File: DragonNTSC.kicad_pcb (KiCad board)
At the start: 2 copper layers, 120.2 x 35.7 mm, 19 parts, among them IC1 74LS273N, IC2 MC6847, IC3 MC1372, J1 Video Output, J2 Board Interconnect Male, Q1 2N4403, Q2 2N4401

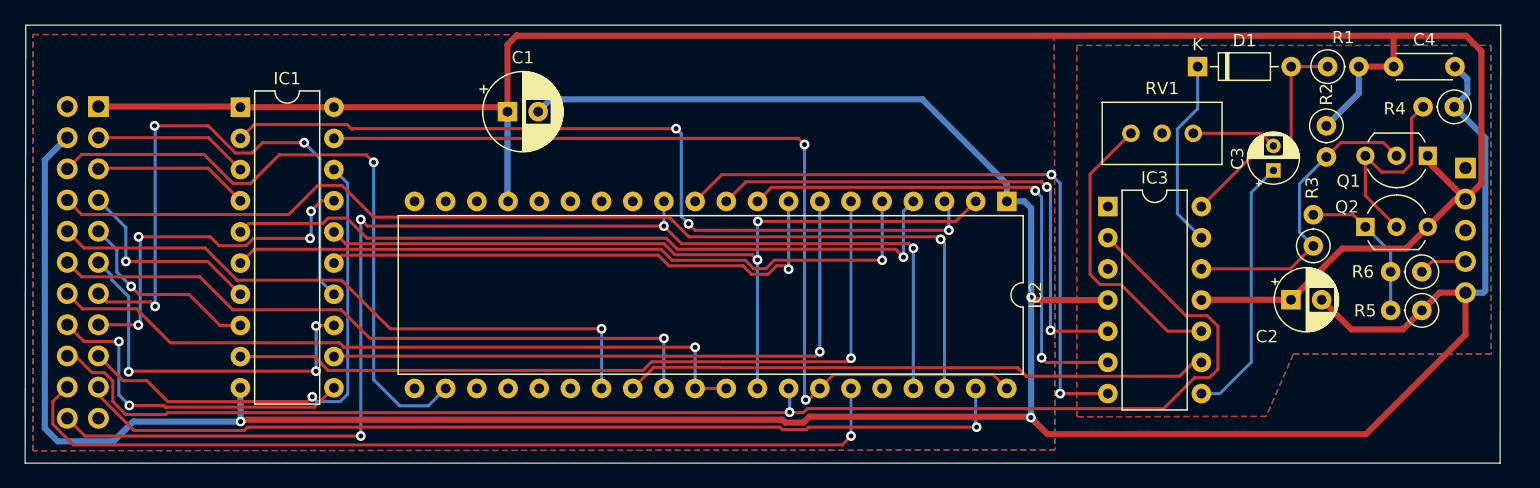
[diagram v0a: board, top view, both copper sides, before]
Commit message: complete tracing for fabrication
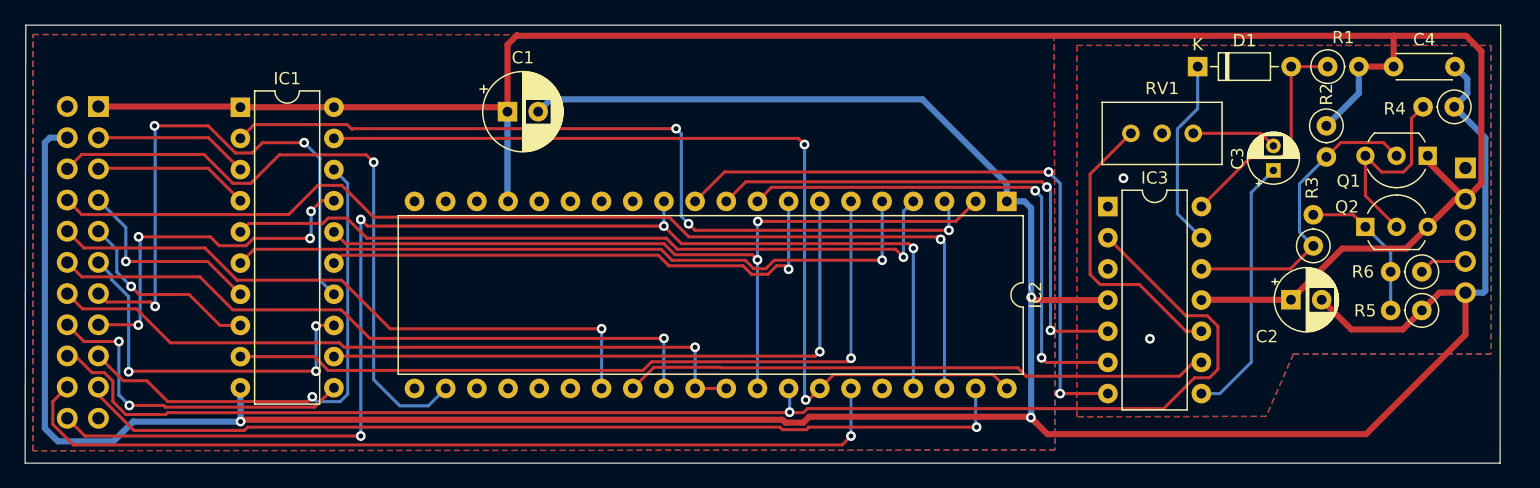
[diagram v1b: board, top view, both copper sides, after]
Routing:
- net GND: track 257.2 -> 258.1 mm, vias 3 -> 5
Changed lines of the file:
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@@
   (segment (start 198.6788 122.2248) (end 198.6788 118.7958) (width 0.5) (layer "F.Cu") (net 2))
   (via (at 163.2712 128.9691) (size 0.8) (drill 0.4) (layers "F.Cu" "B.Cu") (net 2))
+  (via (at 172.974 122.555) (size 0.8) (drill 0.4) (layers "F.Cu" "B.Cu") (free) (net 2))
   (via (at 163.2966 119.1768) (size 0.8) (drill 0.4) (layers "F.Cu" "B.Cu") (net 2))
+  (via (at 170.815 109.474) (size 0.8) (drill 0.4) (layers "F.Cu" "B.Cu") (free) (net 2))
   (via (at 98.8822 129.2993) (size 0.8) (drill 0.4) (layers "F.Cu" "B.Cu") (net 2))
   (segment (start 186.9648 119.8684) (end 186.9648 119.375) (width 0.5) (layer "B.Cu") (net 2))
-  (segment (start 82.931 108.0008) (end 84.7598 106.172) (width 0.5) (layer "B.Cu") (net 2))
   (segment (start 197.826 100.3808) (end 198.8312 101.386) (width 0.5) (layer "B.Cu") (net 2))
+  (segment (start 90.1313 129.2993) (end 88.519 130.9116) (width 0.5) (layer "B.Cu") (net 2))
   (segment (start 98.8822 127.9906) (end 98.8668 127.9752) (width 0.5) (layer "B.Cu") (net 2))
-  (segment (start 83.9978 130.9116) (end 82.931 129.8448) (width 0.5) (layer "B.Cu") (net 2))
   (segment (start 200.3044 106.1938) (end 200.3044 118.618) (width 0.5) (layer "B.Cu") (net 2))
   (segment (start 162.7455 111.3613) (end 161.3154 111.3613) (width 0.5) (layer "B.Cu") (net 2))
   (segment (start 163.2712 128.9691) (end 163.2966 128.9437) (width 0.5) (layer "B.Cu") (net 2))
   (segment (start 198.8312 101.386) (end 198.8312 102.5942) (width 0.5) (layer "B.Cu") (net 2))
-  (segment (start 82.931 129.8448) (end 82.931 108.0008) (width 0.5) (layer "B.Cu") (net 2))
+  (segment (start 83.9978 130.9116) (end 82.931 129.8448) (width 0.5) (layer "B.Cu") (net 2))
   (segment (start 88.519 130.9116) (end 83.9978 130.9116) (width 0.5) (layer "B.Cu") (net 2))
   (segment (start 198.8312 102.5942) (end 197.768 103.6574) (width 0.5) (layer "B.Cu") (net 2))
@@
   (segment (start 163.2966 119.1768) (end 163.2966 111.9124) (width 0.5) (layer "B.Cu") (net 2))
   (segment (start 200.3044 118.618) (end 200.1266 118.7958) (width 0.5) (layer "B.Cu") (net 2))
+  (segment (start 82.931 106.5784) (end 83.3374 106.172) (width 0.5) (layer "B.Cu") (net 2))
+  (segment (start 83.3374 106.172) (end 84.7598 106.172) (width 0.5) (layer "B.Cu") (net 2))
   (segment (start 98.8668 127.9752) (end 98.8668 126.5478) (width 0.5) (layer "B.Cu") (net 2))
+  (segment (start 82.931 129.8448) (end 82.931 106.5784) (width 0.5) (layer "B.Cu") (net 2))
+  (segment (start 98.8822 129.2993) (end 90.1313 129.2993) (width 0.5) (layer "B.Cu") (net 2))
   (segment (start 163.2966 111.9124) (end 162.7455 111.3613) (width 0.5) (layer "B.Cu") (net 2))
   (segment (start 161.3154 109.9312) (end 154.432 103.0478) (width 0.5) (layer "B.Cu") (net 2))
@@
   (segment (start 200.1266 118.7958) (end 198.6788 118.7958) (width 0.5) (layer "B.Cu") (net 2))
   (segment (start 163.2712 128.9691) (end 163.7405 129.4384) (width 0.5) (layer "B.Cu") (net 2))
-  (segment (start 90.1313 129.2993) (end 88.519 130.9116) (width 0.5) (layer "B.Cu") (net 2))
   (segment (start 98.8822 129.2993) (end 98.8822 127.9906) (width 0.5) (layer "B.Cu") (net 2))
   (segment (start 154.432 103.0478) (end 124.1329 103.0478) (width 0.5) (layer "B.Cu") (net 2))
-  (segment (start 98.8822 129.2993) (end 90.1313 129.2993) (width 0.5) (layer "B.Cu") (net 2))
   (segment (start 163.2966 128.9437) (end 163.2966 119.1768) (width 0.5) (layer "B.Cu") (net 2))
   (segment (start 107.5666 105.1028) (end 99.9918 105.1028) (width 0.25) (layer "F.Cu") (net 3))
@@
   (segment (start 164.8706 110.480803) (end 164.8706 121.8692) (width 0.25) (layer "B.Cu") (net 21))
   (segment (start 164.580134 110.190337) (end 164.8706 110.480803) (width 0.25) (layer "B.Cu") (net 21))
-  (segment (start 138.0948 109.1819) (end 135.9154 111.3613) (width 0.25) (layer "F.Cu") (net 22))
-  (segment (start 164.9476 109.1819) (end 138.0948 109.1819) (width 0.25) (layer "F.Cu") (net 22))
+  (segment (start 164.719 108.966) (end 138.3107 108.966) (width 0.25) (layer "F.Cu") (net 22))
   (segment (start 165.6588 127.0204) (end 169.545 127.0204) (width 0.25) (layer "F.Cu") (net 22))
-  (via (at 164.9476 109.1819) (size 0.8) (drill 0.4) (layers "F.Cu" "B.Cu") (net 22))
+  (segment (start 138.3107 108.966) (end 135.9154 111.3613) (width 0.25) (layer "F.Cu") (net 22))
+  (via (at 164.719 108.966) (size 0.8) (drill 0.4) (layers "F.Cu" "B.Cu") (net 22))
   (via (at 165.6588 127.0204) (size 0.8) (drill 0.4) (layers "F.Cu" "B.Cu") (net 22))
-  (segment (start 165.6588 127.0204) (end 165.6588 109.8931) (width 0.25) (layer "B.Cu") (net 22))
-  (segment (start 165.6588 109.8931) (end 164.9476 109.1819) (width 0.25) (layer "B.Cu") (net 22))
+  (segment (start 165.6588 109.9058) (end 165.6588 127.0204) (width 0.25) (layer "B.Cu") (net 22))
+  (segment (start 164.719 108.966) (end 165.6588 109.9058) (width 0.25) (layer "B.Cu") (net 22))
   (segment (start 133.371101 113.3735) (end 134.805601 114.808) (width 0.25) (layer "F.Cu") (net 23))
   (segment (start 153.328824 114.808) (end 153.7004 115.179576) (width 0.25) (layer "F.Cu") (net 23))
@@
   (segment (start 158.7754 126.6013) (end 158.7754 129.6783) (width 0.25) (layer "B.Cu") (net 45))
   (segment (start 158.7754 129.6783) (end 158.8516 129.7545) (width 0.25) (layer "B.Cu") (net 45))
-  (segment (start 168.917105 118.1354) (end 170.6118 118.1354) (width 0.25) (layer "F.Cu") (net 48))
+  (segment (start 171.4246 105.8164) (end 168.0972 109.1438) (width 0.25) (layer "F.Cu") (net 48))
+  (segment (start 168.917105 118.1354) (end 172.1104 118.1354) (width 0.25) (layer "F.Cu") (net 48))
+  (segment (start 172.1104 118.1354) (end 175.9154 121.9404) (width 0.25) (layer "F.Cu") (net 48))
   (segment (start 168.0972 117.315495) (end 168.917105 118.1354) (width 0.25) (layer "F.Cu") (net 48))
+  (segment (start 175.9154 121.9404) (end 177.165 121.9404) (width 0.25) (layer "F.Cu") (net 48))
   (segment (start 168.0972 109.1438) (end 168.0972 117.315495) (width 0.25) (layer "F.Cu") (net 48))
-  (segment (start 170.6118 118.1354) (end 174.4168 121.9404) (width 0.25) (layer "F.Cu") (net 48))
-  (segment (start 171.4246 105.8164) (end 168.0972 109.1438) (width 0.25) (layer "F.Cu") (net 48))
-  (segment (start 174.4168 121.9404) (end 177.165 121.9404) (width 0.25) (layer "F.Cu") (net 48))
   (segment (start 195.9646 116.2558) (end 195.1264 117.094) (width 0.25) (layer "F.Cu") (net 49))
   (segment (start 198.6788 116.2558) (end 195.9646 116.2558) (width 0.25) (layer "F.Cu") (net 49))

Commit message: prepare alpha2 build
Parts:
- added C5: 150pF, Capacitor_THT:C_Rect_L7.0mm_W2.5mm_P5.00mm, F.Cu at (164.4, 130.8)
- added C6: 0.1uF, Capacitor_THT:C_Rect_L7.0mm_W2.5mm_P5.00mm, F.Cu at (149.9, 104.0)
- added FB1: ?uH, Inductor_THT:L_Axial_L7.0mm_D3.3mm_P5.08mm_Vertical_Fastron_MICC, F.Cu at (119.4, 129.6)
- added R7: 150R, Resistor_THT:R_Axial_DIN0207_L6.3mm_D2.5mm_P2.54mm_Vertical, F.Cu at (142.3, 129.2)
- added R8: 10k, Resistor_THT:R_Axial_DIN0207_L6.3mm_D2.5mm_P2.54mm_Vertical, F.Cu at (157.5, 129.5)
- moved R4 8.19 mm to (190.6, 107.6), turned to 0 degrees
- moved R2 5.83 mm to (186.5, 111.0)
- moved C2 5.82 mm to (184.5, 125.2)
- moved D1 5.04 mm to (178.9, 105.0)
- moved C4 4.54 mm to (194.5, 104.6)
- moved R1 4.47 mm to (189.6, 104.3)
- moved C3 3.88 mm to (182.5, 112.7)
- moved R5 3.73 mm to (195.1, 124.0)
- moved Q1 3.45 mm to (195.6, 111.1)
- moved Q2 3.25 mm to (190.6, 116.7)
- moved R6 3.18 mm to (195.1, 120.3)
- moved R3 3.14 mm to (183.7, 116.8), turned to 0 degrees
- moved RV1 1.57 mm to (174.9, 105.8)
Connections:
- net Net-(IC1-Q0) renamed /D0
- net Net-(IC1-Q1) renamed /D1
- net Net-(IC1-Q2) renamed /D2
- net Net-(IC1-Q3) renamed /D3
- net Net-(IC1-Q4) renamed /D4
- net Net-(IC1-Q5) renamed /D5
- net Net-(IC1-Q6) renamed /D6
- net Net-(IC1-Q7) renamed /D7
- IC2 pad 33: VCLK -> Net-(IC2-CLK)
- IC3 pad 2: VCLK -> Net-(IC3-OSC)
- J2 pad 18: VCLK -> Net-(J2-Pin_18)
- RV1 pad 1: Net-(C3-Pad2) -> unconnected-(RV1-Pad1)
- RV1 pad 2: unconnected-(RV1-Pad2) -> Net-(C3-Pad2)
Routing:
- net GND: track 258.1 -> 45.5 mm, vias 5 -> 8
- net +5V: track 180.1 -> 0.00 mm
- net VCLK: track 115.7 -> 34.2 mm, vias 1 -> 0
- net Net-(J2-Pin_18): track 0.00 -> 38.0 mm
- net Net-(IC3-OSC): track 0.00 -> 35.8 mm
- net /D6: track 67.5 -> 86.1 mm, vias 2 -> 3
- net CSS: track 76.9 -> 86.2 mm, vias 1 -> 0
- net Composite: track 25.2 -> 19.5 mm
- net Net-(C3-Pad2): track 6.95 -> 12.1 mm
- net phiA: track 52.1 -> 56.4 mm, vias 2 -> 0
- net /D7: track 77.1 -> 81.2 mm, vias 2 -> 1
- net Net-(IC3-ChrMod): track 21.5 -> 17.4 mm
- net Net-(D1-K): track 15.4 -> 11.7 mm
- net Net-(IC2-CLK): track 0.00 -> 3.19 mm
- net LUM: track 47.8 -> 50.9 mm
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- added copper zone on In2.Cu, net +5V
- added copper zone on In1.Cu, net GND
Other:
- board size 120.2 x 35.7 mm -> 120.2 x 32.4 mm
- copper layers 2 -> 4
- board text added: "Dragon 32 Rev 3 NTSC"

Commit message: update
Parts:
- added C7: 22nF, Capacitor_THT:C_Rect_L7.0mm_W2.5mm_P5.00mm, F.Cu at (136.4, 101.8)
- added C8: 22nF, Capacitor_THT:C_Rect_L7.0mm_W2.5mm_P5.00mm, F.Cu at (95.3, 100.3)
- added C9: 0.1uF, Capacitor_THT:C_Rect_L7.0mm_W2.5mm_P5.00mm, F.Cu at (99.9, 99.2)
- added D2: 1N3064, Diode_THT:D_DO-35_SOD27_P7.62mm_Horizontal, F.Cu at (112.9, 101.4)
- added IC4: LM555xN, Package_DIP:DIP-8_W7.62mm, F.Cu at (133.3, 99.4)
- added Q3: 2N4401, Package_TO_SOT_THT:TO-92_Inline_Wide, F.Cu at (139.0, 103.5)
- added R10: 2K2, Resistor_THT:R_Axial_DIN0207_L6.3mm_D2.5mm_P2.54mm_Vertical, F.Cu at (108.0, 99.2)
- added R11: 47K, Resistor_THT:R_Axial_DIN0207_L6.3mm_D2.5mm_P2.54mm_Vertical, F.Cu at (152.1, 99.6)
- added R12: 1K, Resistor_THT:R_Axial_DIN0207_L6.3mm_D2.5mm_P2.54mm_Vertical, F.Cu at (146.8, 101.4)
- added R9: 2K2, Resistor_THT:R_Axial_DIN0207_L6.3mm_D2.5mm_P2.54mm_Vertical, F.Cu at (87.4, 100.3)
- C2: value 1uF -> 10uF
- moved C1 3.44 mm to (120.7, 107.5), turned to 90 degrees
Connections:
- C4 pad 1: +5V -> unconnected-(C4-Pad1)
- J1 pad 3: unconnected-(J1-Pin_3-Pad3) -> -5V
- J2 pad 2: -5V -> ~{RES}
- J2 pad 21: unconnected-(J2-Pin_21-Pad21) -> GND
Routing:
- net Net-(IC4-CV): track 0.00 -> 43.1 mm
- net Net-(D2-A): track 0.00 -> 33.0 mm
- net CSS: track 86.2 -> 117.0 mm, vias 0 -> 1
- net Net-(IC4-DIS): track 0.00 -> 30.3 mm
- net Net-(IC4-Q): track 0.00 -> 25.1 mm
- net GM0: track 61.0 -> 84.8 mm
- net ~{HS}: track 86.6 -> 100.4 mm, vias 1 -> 2
- net GND: track 45.5 -> 57.3 mm, vias 8 -> 44
- net Net-(Q3-C): track 0.00 -> 3.57 mm
- net /D0: track 68.3 -> 65.8 mm
- net phiA: track 56.4 -> 58.9 mm
- net /D7: track 81.2 -> 78.9 mm
- net ~{FS}: track 102.9 -> 101.5 mm
- net CHB: track 43.8 -> 42.5 mm
- net phiB: track 45.5 -> 44.7 mm
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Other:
- board size 120.2 x 32.4 mm -> 120.2 x 35.1 mm
